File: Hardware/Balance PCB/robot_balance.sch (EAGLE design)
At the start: 52 parts, among them P1 10118194-0001LF, Q1 16Mhz

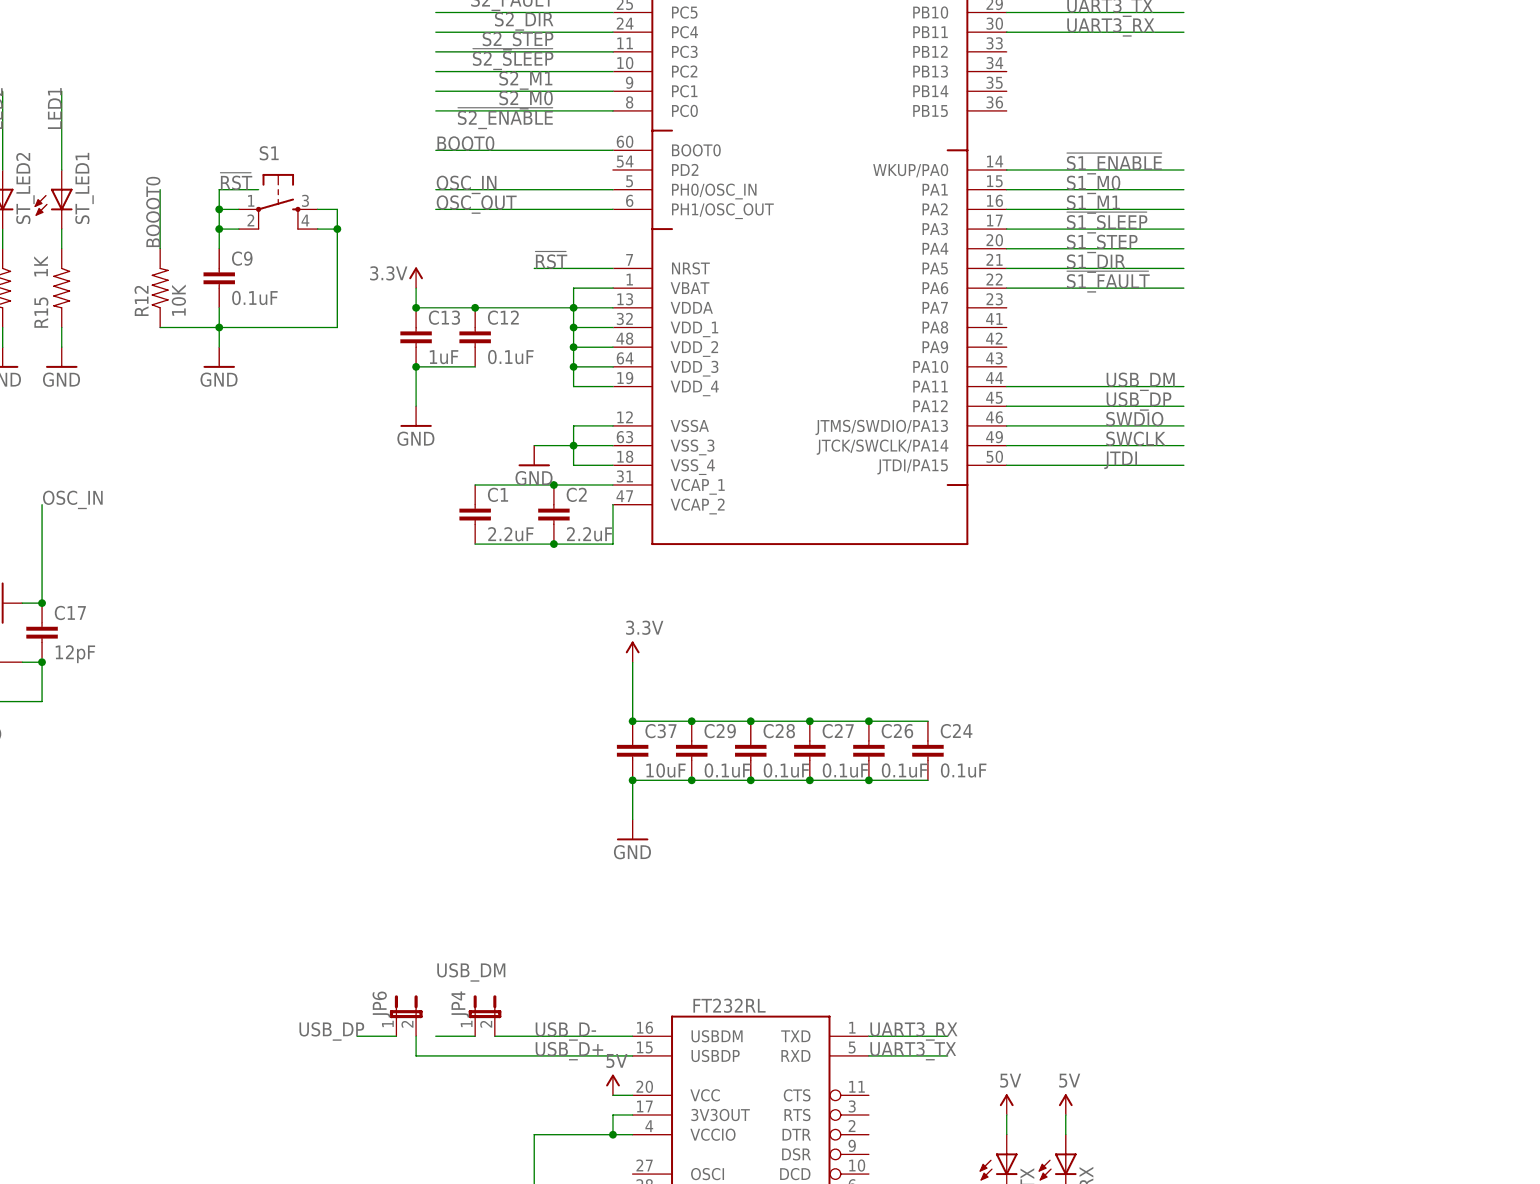
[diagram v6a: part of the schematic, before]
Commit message: Layout changed slightly and labels placed
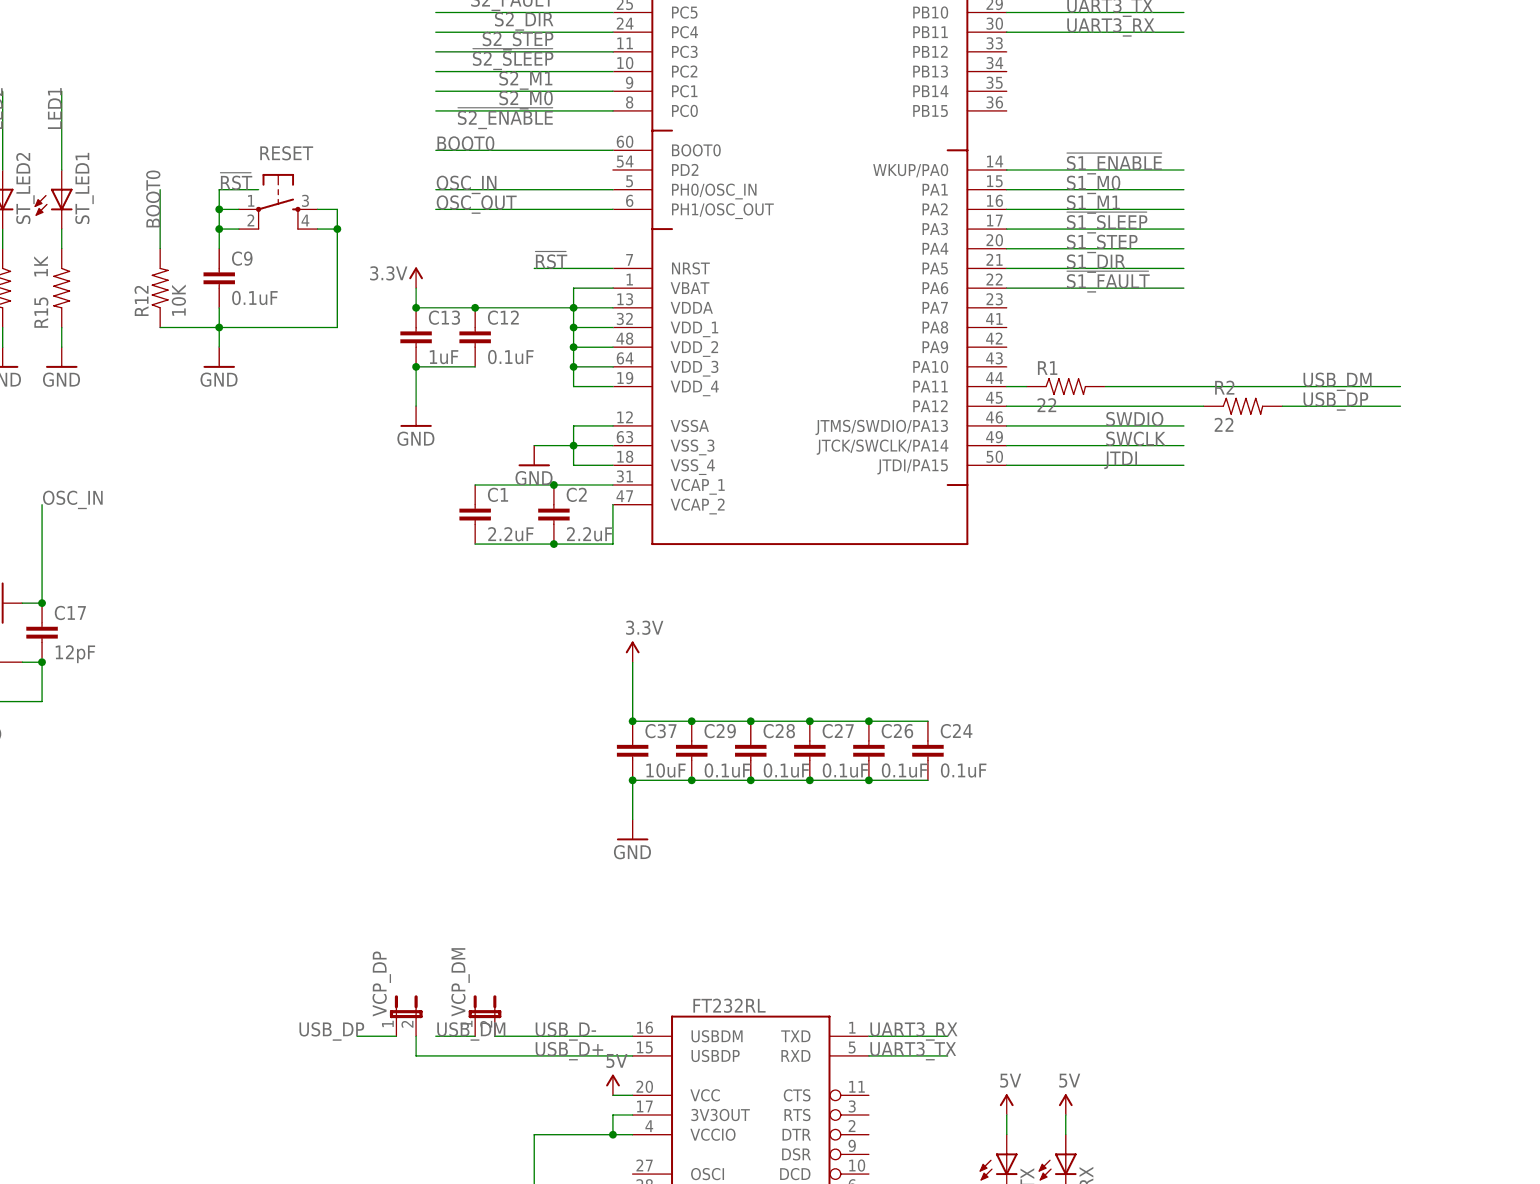
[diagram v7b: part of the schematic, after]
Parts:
- added R1, R2: 22, SparkFun-Passives:RESISTOR0805-RES
- renumbered JP4 to VCP_DM, JP6 to VCP_DP, S1 to RESET
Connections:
- removed net BOOOT0: R12.2
- new net N$14: R2.1, U$4.PA12
- new net N$7: R1.1, U$4.PA11
- net BOOT0: now also R12.2
- net USB_DM: now also R1.2; no longer U$4.PA11
- net USB_DP: now also R2.2; no longer U$4.PA12
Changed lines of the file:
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@@
 <part name="C2" library="SparkFun-Capacitors" deviceset="2.2UF-25V-+80/-20(0805)" device="" value="2.2uF"/>
 <part name="SUPPLY1" library="SparkFun-Aesthetics" deviceset="3.3V" device=""/>
-<part name="S1" library="SparkFun-Electromechanical" deviceset="TAC_SWITCH" device="SMD"/>
+<part name="RESET" library="SparkFun-Electromechanical" deviceset="TAC_SWITCH" device="SMD"/>
 <part name="C9" library="SparkFun-Capacitors" deviceset="2.2UF-25V-+80/-20(0805)" device="" value="0.1uF"/>
 <part name="GND8" library="SparkFun-Aesthetics" deviceset="GND" device=""/>
@@
 <part name="SUPPLY14" library="SparkFun-Aesthetics" deviceset="3.3V" device=""/>
 <part name="R_EN" library="SparkFun-Passives" deviceset="RESISTOR" device="0603-RES" value="1K"/>
-<part name="JP4" library="SparkFun-Retired" deviceset="JUMPER-2" device="SMD-NO"/>
-<part name="JP6" library="SparkFun-Retired" deviceset="JUMPER-2" device="SMD-NO"/>
+<part name="VCP_DM" library="SparkFun-Retired" deviceset="JUMPER-2" device="SMD-NO"/>
+<part name="VCP_DP" library="SparkFun-Retired" deviceset="JUMPER-2" device="SMD-NO"/>
+<part name="R1" library="SparkFun-Passives" deviceset="RESISTOR" device="0805-RES" value="22"/>
+<part name="R2" library="SparkFun-Passives" deviceset="RESISTOR" device="0805-RES" value="22"/>
 </parts>
 <sheets>
@@
 <instance part="C2" gate="G$1" x="58.42" y="-88.9"/>
 <instance part="SUPPLY1" gate="G$1" x="68.58" y="-106.68"/>
-<instance part="S1" gate="S" x="22.86" y="-48.26"/>
+<instance part="RESET" gate="S" x="22.86" y="-48.26"/>
 <instance part="C9" gate="G$1" x="15.24" y="-58.42"/>
 <instance part="GND8" gate="1" x="15.24" y="-68.58"/>
@@
 <instance part="SUPPLY14" gate="G$1" x="226.06" y="-68.58"/>
 <instance part="R_EN" gate="G$1" x="33.02" y="-12.7"/>
-<instance part="JP4" gate="A" x="48.26" y="-152.4"/>
-<instance part="JP6" gate="A" x="38.1" y="-152.4"/>
+<instance part="VCP_DM" gate="A" x="48.26" y="-152.4"/>
+<instance part="VCP_DP" gate="A" x="38.1" y="-152.4"/>
+<instance part="R1" gate="G$1" x="124.46" y="-71.12"/>
+<instance part="R2" gate="G$1" x="147.32" y="-73.66"/>
 </instances>
 <busses>
@@
 <pinref part="GND8" gate="1" pin="GND"/>
 <wire x1="15.24" y1="-66.04" x2="15.24" y2="-63.5" width="0.1524" layer="91"/>
-<pinref part="S1" gate="S" pin="4"/>
+<pinref part="RESET" gate="S" pin="4"/>
 <wire x1="15.24" y1="-63.5" x2="15.24" y2="-60.96" width="0.1524" layer="91"/>
 <wire x1="27.94" y1="-50.8" x2="30.48" y2="-50.8" width="0.1524" layer="91"/>
 <wire x1="30.48" y1="-50.8" x2="30.48" y2="-48.26" width="0.1524" layer="91"/>
-<pinref part="S1" gate="S" pin="3"/>
+<pinref part="RESET" gate="S" pin="3"/>
 <wire x1="30.48" y1="-48.26" x2="27.94" y2="-48.26" width="0.1524" layer="91"/>
 <wire x1="30.48" y1="-50.8" x2="30.48" y2="-63.5" width="0.1524" layer="91"/>
@@
 <net name="!RST" class="0">
 <segment>
-<pinref part="S1" gate="S" pin="1"/>
+<pinref part="RESET" gate="S" pin="1"/>
 <junction x="15.24" y="-48.26"/>
 <wire x1="15.24" y1="-48.26" x2="17.78" y2="-48.26" width="0.1524" layer="91"/>
-<pinref part="S1" gate="S" pin="2"/>
+<pinref part="RESET" gate="S" pin="2"/>
 <wire x1="17.78" y1="-50.8" x2="15.24" y2="-50.8" width="0.1524" layer="91"/>
 <wire x1="15.24" y1="-50.8" x2="15.24" y2="-48.26" width="0.1524" layer="91"/>
@@
 </segment>
 </net>
-<net name="BOOOT0" class="0">
-<segment>
-<pinref part="R12" gate="G$1" pin="2"/>
-<wire x1="7.62" y1="-53.34" x2="7.62" y2="-45.72" width="0.1524" layer="91"/>
-<label x="7.62" y="-53.34" size="1.778" layer="95" rot="R90"/>
-</segment>
-</net>
 <net name="ARDUINO_TX" class="1">
 <segment>
@@
 <label x="43.18" y="-40.64" size="1.778" layer="95"/>
 </segment>
+<segment>
+<pinref part="R12" gate="G$1" pin="2"/>
+<wire x1="7.62" y1="-53.34" x2="7.62" y2="-45.72" width="0.1524" layer="91"/>
+<label x="7.62" y="-50.8" size="1.778" layer="95" rot="R90"/>
+</segment>
 </net>
 <net name="UART3_TX" class="0">
@@
 <wire x1="50.8" y1="-154.94" x2="68.58" y2="-154.94" width="0.1524" layer="91"/>
 <label x="55.88" y="-154.94" size="1.778" layer="95"/>
-<pinref part="JP4" gate="A" pin="2"/>
+<pinref part="VCP_DM" gate="A" pin="2"/>
 </segment>
 <segment>
@@
 <pinref part="FT232RL" gate="G$1" pin="USBDP"/>
 <label x="55.88" y="-157.48" size="1.778" layer="95"/>
-<pinref part="JP6" gate="A" pin="2"/>
+<pinref part="VCP_DP" gate="A" pin="2"/>
 <wire x1="68.58" y1="-157.48" x2="40.64" y2="-157.48" width="0.1524" layer="91"/>
 <wire x1="40.64" y1="-157.48" x2="40.64" y2="-154.94" width="0.1524" layer="91"/>
@@
 <net name="USB_DM" class="0">
 <segment>
-<pinref part="JP4" gate="A" pin="1"/>
+<pinref part="VCP_DM" gate="A" pin="1"/>
 <wire x1="48.26" y1="-154.94" x2="43.18" y2="-154.94" width="0.1524" layer="91"/>
-<label x="43.18" y="-147.32" size="1.778" layer="95"/>
-</segment>
-<segment>
-<pinref part="U$4" gate="G$1" pin="PA11"/>
-<wire x1="116.84" y1="-71.12" x2="139.7" y2="-71.12" width="0.1524" layer="91"/>
-<label x="129.54" y="-71.12" size="1.778" layer="95"/>
+<label x="43.18" y="-154.94" size="1.778" layer="95"/>
+</segment>
+<segment>
+<wire x1="129.54" y1="-71.12" x2="167.64" y2="-71.12" width="0.1524" layer="91"/>
+<label x="154.94" y="-71.12" size="1.778" layer="95"/>
+<pinref part="R1" gate="G$1" pin="2"/>
 </segment>
 </net>
 <net name="USB_DP" class="0">
 <segment>
-<pinref part="JP6" gate="A" pin="1"/>
+<pinref part="VCP_DP" gate="A" pin="1"/>
 <wire x1="38.1" y1="-154.94" x2="33.02" y2="-154.94" width="0.1524" layer="91"/>
 <label x="25.4" y="-154.94" size="1.778" layer="95"/>
 </segment>
 <segment>
+<wire x1="152.4" y1="-73.66" x2="167.64" y2="-73.66" width="0.1524" layer="91"/>
+<label x="154.94" y="-73.66" size="1.778" layer="95"/>
+<pinref part="R2" gate="G$1" pin="2"/>
+</segment>
+</net>
+<net name="N$7" class="0">
+<segment>
+<pinref part="U$4" gate="G$1" pin="PA11"/>
+<pinref part="R1" gate="G$1" pin="1"/>
+<wire x1="119.38" y1="-71.12" x2="116.84" y2="-71.12" width="0.1524" layer="91"/>
+</segment>
+</net>
+<net name="N$14" class="0">
+<segment>
 <pinref part="U$4" gate="G$1" pin="PA12"/>
-<wire x1="116.84" y1="-73.66" x2="139.7" y2="-73.66" width="0.1524" layer="91"/>
-<label x="129.54" y="-73.66" size="1.778" layer="95"/>
-</segment>
-</net>
+<pinref part="R2" gate="G$1" pin="1"/>
+<wire x1="142.24" y1="-73.66" x2="116.84" y2="-73.66" width="0.1524" layer="91"/>
+</segment>
+</net>
